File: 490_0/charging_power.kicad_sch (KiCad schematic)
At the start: 32 parts, among them J8 S2B-XH-A, J9 USB_C_Receptacle_USB2.0_16P, SW2 SW_Push, SW3 SW_Push, U4 MP2632BGR-Z

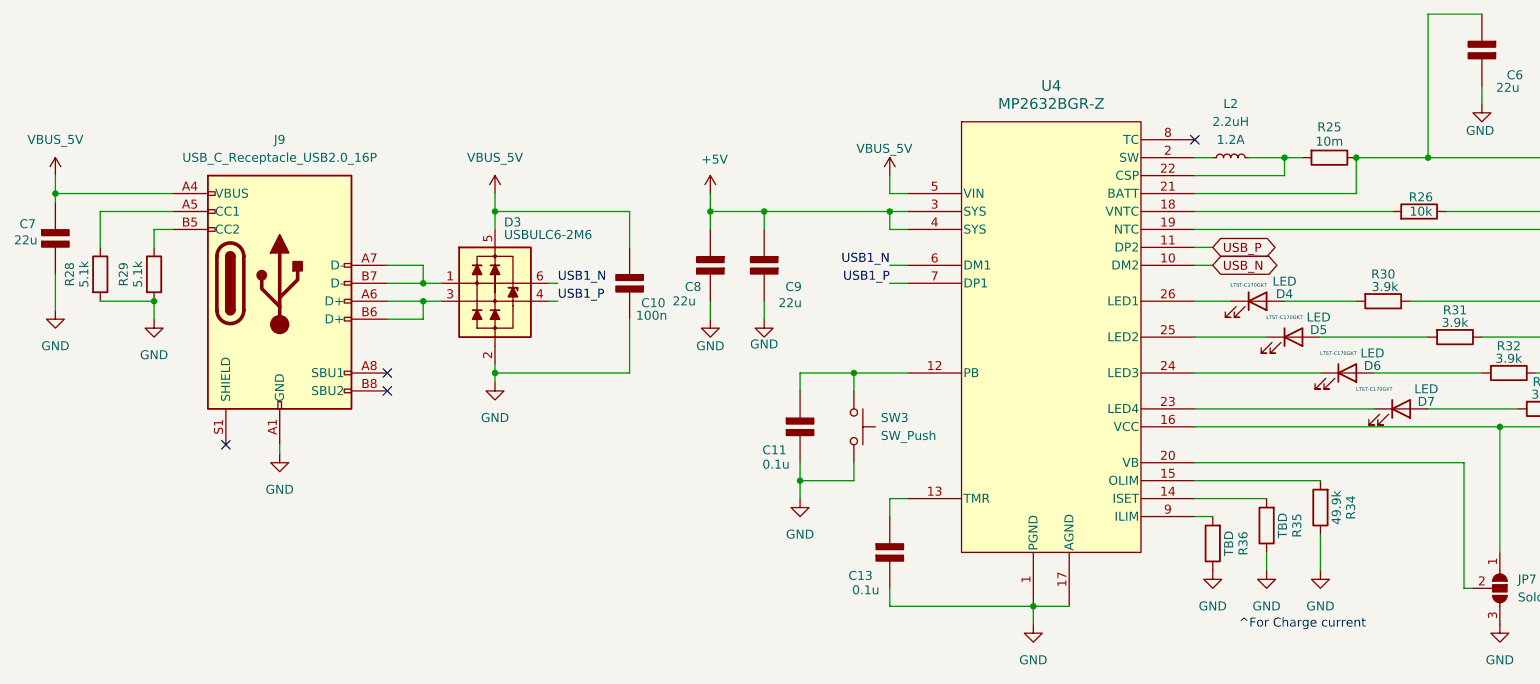
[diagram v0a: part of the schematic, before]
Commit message: changed PCB block diagram
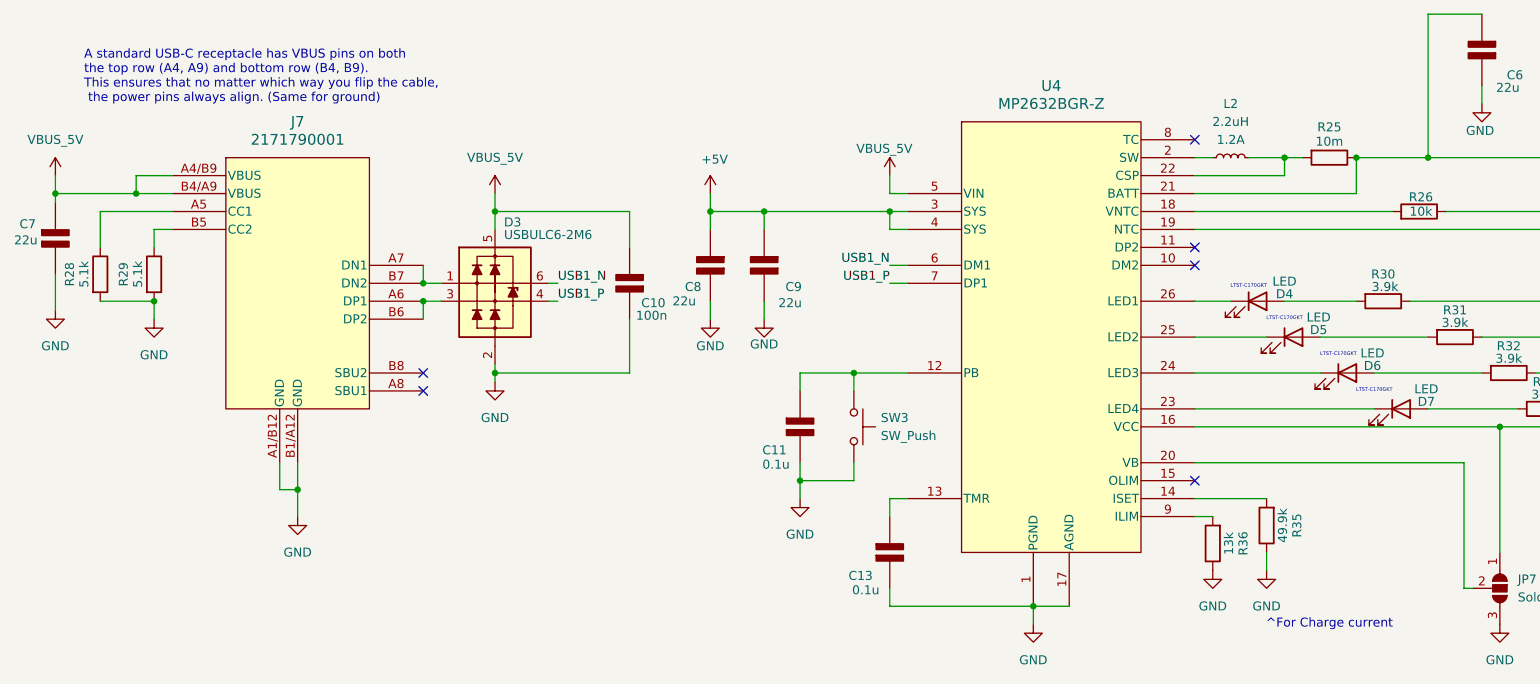
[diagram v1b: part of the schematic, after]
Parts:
- removed J9: USB_C_Receptacle_USB2.0_16P, symbol Connector:USB_C_Receptacle_USB2.0_16P
- removed R34: 49.9k, symbol Device:R
- added J7: 2171790001, 2171790001_MOL, symbol capstone_parts:2171790001
- R35: value TBD -> 49.9k
- R36: value TBD -> 13k
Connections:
- net GND: now also J7.A1/B12 (GND), J7.B1/A12 (GND)
- net VBUS_5V: now also J7.A4/B9 (VBUS), J7.B4/A9 (VBUS)
- net at R29.1: now also J7.B5 (CC2)
- net at R28.1: now also J7.A5 (CC1)
- net at D3.3 (L2): now also J7.A6 (DP1), J7.B6 (DP2)
- net at D3.1 (L1): now also J7.A7 (DN1), J7.B7 (DN2)
- net USB_N: no longer names the net of U4.10 (DM2)
- net USB_P: no longer names the net of U4.11 (DP2)
- no-connect marks 4 -> 6
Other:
- note added: "A standard USB-C receptacle has VBUS pins on both the top row (A4, A9) and bottom row (B4, B9). This ensures that no matter which way you flip the cable, the power pins always align. (Same for ground)"

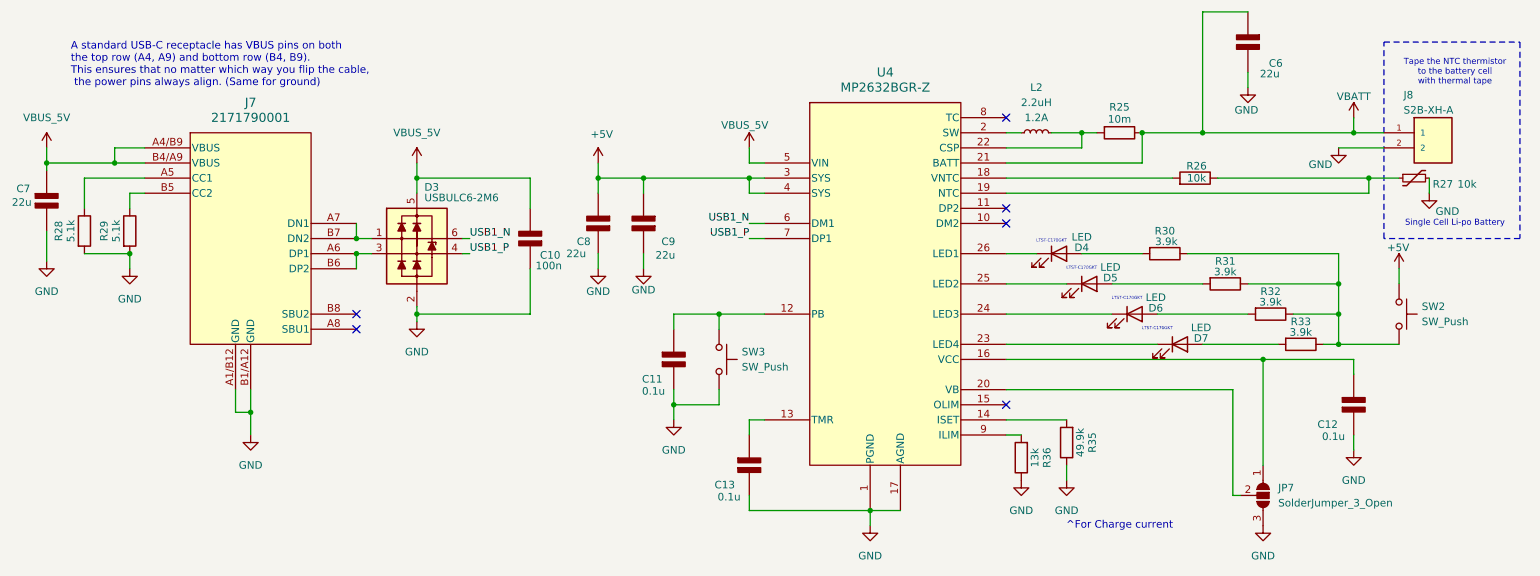
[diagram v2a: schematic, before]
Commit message: Schematic layout update
- applied hierarchical labels
- cleaned up the schematic
- finalized CM4 connections
- checked cm4 connections
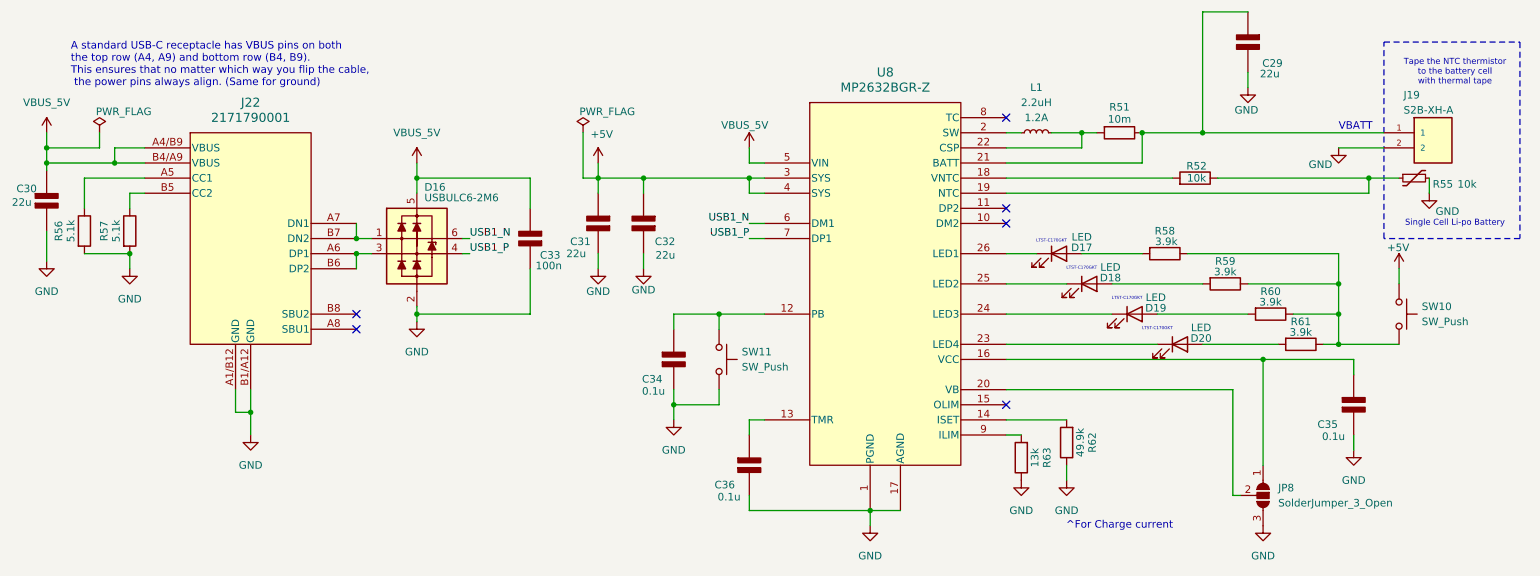
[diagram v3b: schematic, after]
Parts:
- renumbered C6 to C29, C7 to C30, C8 to C31, C9 to C32, C10 to C33, C11 to C34, C12 to C35, C13 to C36, D3 to D16, D4 to D17, D5 to D18, D6 to D19, D7 to D20, J8 to J19, J7 to J22, JP7 to JP8, L2 to L1, R25 to R51, R26 to R52, R27 to R55, R28 to R56, R29 to R57, R30 to R58, R31 to R59, R32 to R60, R33 to R61, R35 to R62, R36 to R63, SW2 to SW10, SW3 to SW11, U4 to U8
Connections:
- net VBATT: no longer names the net of C29.1 (+), J19.1, R51.1, U8.21 (BATT)
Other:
- note added: "VBATT"

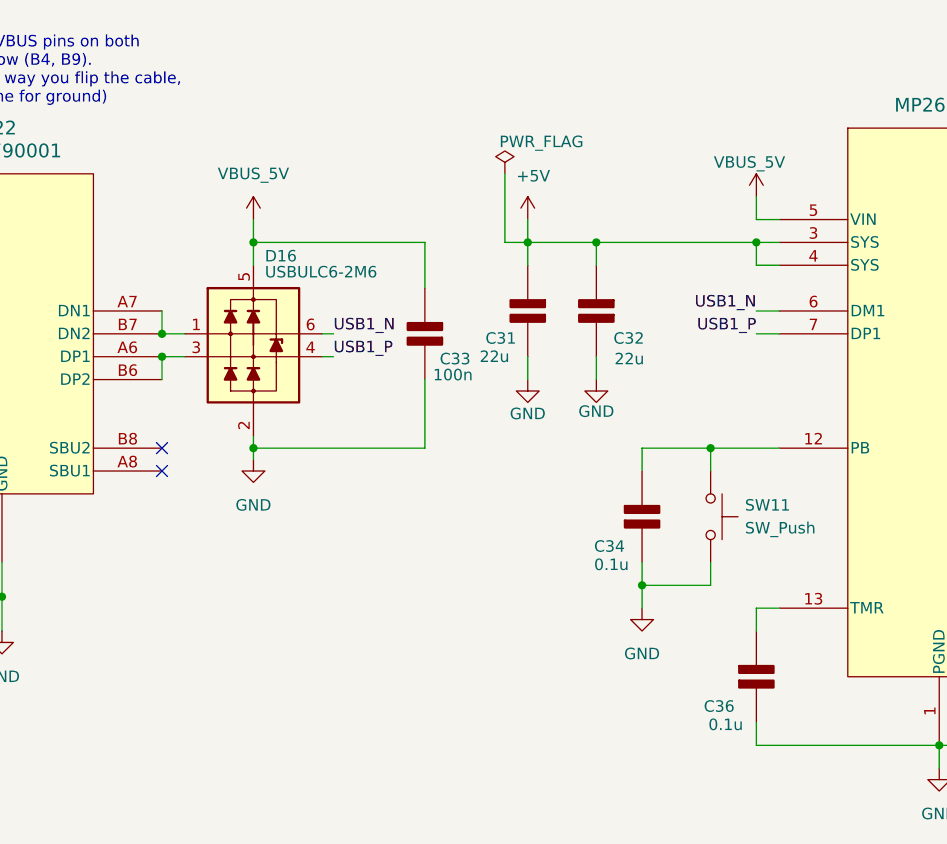
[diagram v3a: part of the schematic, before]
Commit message: Cleaned up global labels
TO DO: power chip change
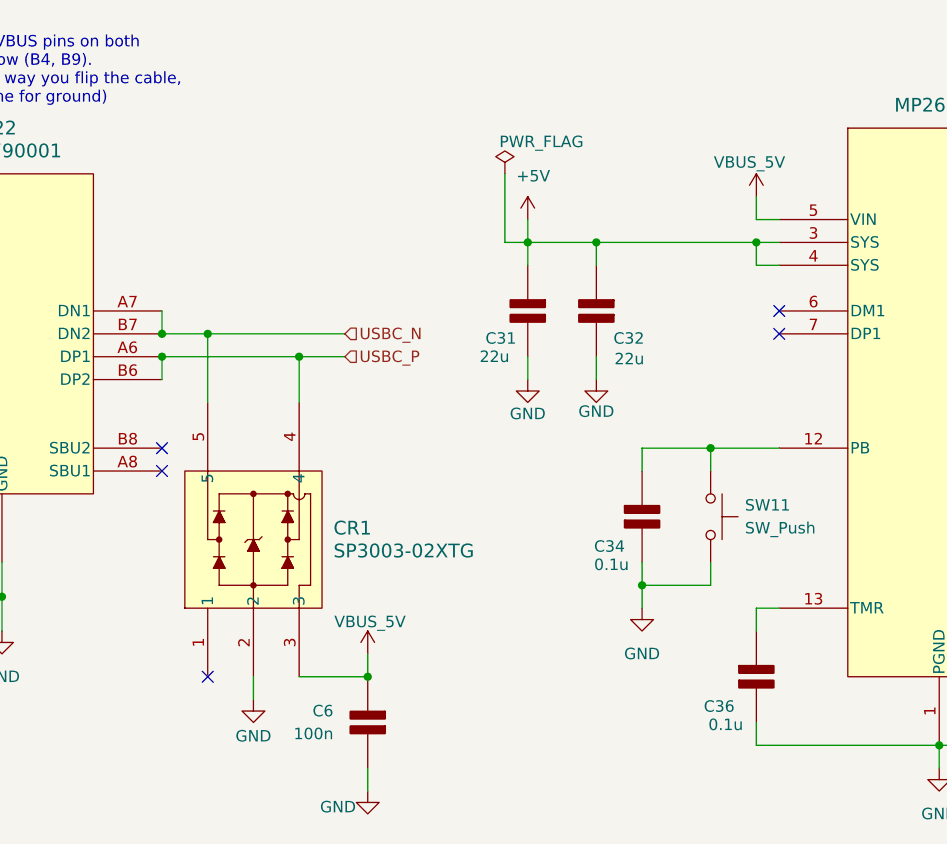
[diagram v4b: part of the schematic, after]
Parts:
- removed C33: 100n, symbol PCM_Elektuur:C
- removed D16: USBULC6-2M6, PCM_Package_TO_SOT_SMD_AKL:SOT-666, symbol PCM_Diode_TVS_AKL:USBLC6-2P6
- added C6: 100n, symbol PCM_Elektuur:C
- added CR1: SP3003-02XTG, SOT553_LTF, symbol capstone_parts:SP3003-02XTG
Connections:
- net GND: now also C6.2 (-), CR1.2
- net VBUS_5V: now also C6.1 (+), CR1.3
- net USBC_P: now reaches J22.A6 (DP1), J22.B6 (DP2)
- net USBC_P: now also CR1.4
- net USBC_N: now reaches J22.A7 (DN1), J22.B7 (DN2)
- net USBC_N: now also CR1.5
- net USB1_N: no longer names the net of U8.6 (DM1)
- net USB1_P: no longer names the net of U8.7 (DP1)
- no-connect marks 6 -> 9

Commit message: Updated power circuit
We now have a 2 cell battery
Chip provides 4A/5V source
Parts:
- added C10, C14: 22u, symbol PCM_Elektuur:C
- added C11, C12, C9: 0.1u, symbol PCM_Elektuur:C
- added C13: 470u, symbol PCM_Elektuur:C
- added C8: 1u, symbol PCM_Elektuur:C
- added D16, D3, D4, D5, D6: LED, symbol Device:LED
- added J18: B3B-XH-A, B3B-XH-A:JST_B3B-XH-A, symbol capstone_parts:B3B-XH-A
- added L2: 2.2u, PCM_SparkFun-Coil:0806, symbol PCM_SparkFun-Coil:2.2uH_0806_1.2A
- added R10: 43k, symbol Device:R
- added R11: 36k, symbol Device:R
- added R12: 82k, symbol Device:R
- added R13: 27k, symbol Device:R
- added R14, R15, R16, R17, R20: 3.9k, symbol Device:R
- added R18, R19, R23: 10k, symbol Device:R
- added R21: 75k, symbol Device:R
- added R22: 24k, symbol Device:R
- added R9: 10k, symbol PCM_SparkFun-Resistor:Thermistor-NTC-10k
- added SW1: SW_Push, symbol Switch:SW_Push
- added TP1: TestPoint, symbol Connector:TestPoint
- added U4: MP2639AGR-Z, symbol capstone_parts:MP2639AGR-Z
- C29, C31, C32, C34, C35, C36, D17, D18, D19, D20, J19, L1, R51, R52, R55, R58, R59, R60, R61, R62, R63, SW10, SW11, U8: now not fitted; now left out of the parts list
- JP8: now not fitted
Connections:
- net VBUS_5V is gone; now on net +5V: C30.1 (+), C6.1 (+), CR1.3, J22.A4/B9 (VBUS), J22.B4/A9 (VBUS), U8.5 (VIN)
- net +5V: now also C13.1 (+), C14.1 (+), R13.1, R21.2, U4.1 (VL)
- net GND: now also C10.1 (+), C12.2 (-), C13.2 (-), C14.2 (-), C8.2 (-), C9.2 (-), J18.3, R10.1, R11.1, R12.1, R18.2, R22.1, R9.2, SW1.2, U4.10 (AGND), U4.5 (PGND)
- new net: R12.2, U4.23 (ISET)
- new net: TP1.1, U4.21 (IB)
- new net: C12.1 (+), SW1.1, U4.7 (PB)
- new net: R10.2, U4.22 (OLIM)
- new net: D5.1 (K), U4.15 (LED3)
- new net: D5.2 (A), R16.2
- new net: D4.1 (K), U4.14 (LED2)
- new net: D4.2 (A), R15.2
- new net: C11.2 (-), L2.1, U4.2 (LX), U4.4 (SW)
- new net: C9.1 (+), U4.11 (TMR)
- new net: D3.1 (K), U4.13 (LED1)
- new net: D3.2 (A), R14.2
- new net: C11.1 (+), U4.6 (BST)
- new net: R14.1, R15.1, R16.1, R17.1, R19.2, R20.1, U4.19 (VNTC)
- new net: J18.2, U4.12 (MID)
- new net: D6.1 (K), U4.16 (LED4)
- new net: R21.1, R22.2, U4.17 (FB)
- new net: R13.2, R18.1, U4.18 (VLIM)
- new net: R19.1, R9.1, U4.20 (NTC)
- new net: R11.2, U4.24 (ILIM)
- new net: R23.1, U4.25 (ACOK), U4.8 (MODE)
- new net: D16.1 (K), U4.26 (CHG)
- new net: C8.1 (+), R23.2, U4.9 (VCC)
- new net: D6.2 (A), R17.2
- new net: D16.2 (A), R20.2
- new net +BATT: C10.2 (-), J18.1, L2.2, U4.3 (VH)
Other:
- note added: ""Anti-Crash" Capacitor (Crucial for CM4)"
- note added: "2 Cell Li-po Battery With thermistor taped on it assemble two 18650 single cell batteries and add the mid point cable between the two"
- note added: "Aluminum Electrolytic (Low ESR)"
- note added: "Charge Current,ISET (23),82 kΩ,~2.6A Charging (Fast for 4Ah cells) Input Limit,ILIM (21),36 kΩ,~3.1A Limit from USB (Safe for most adapters) Discharge Limit,OLIM (22),43 kΩ,~4.9A Limit (for 4A load) Logic Pull-up,ACOK (25),10 kΩ,Standard Pull-up Temp Fake (High),VNTC to NTC,10 kΩ,Part 1 of Voltage Divider Temp Fake (Low),NTC to AGND,10 kΩ,Part 2 of Voltage Divider"
- note added: "USB Inserted: The chip detects 5V on VL. ACOK pulls internal switch to Ground (LOW). -> MODE goes LOW -> Chip enters Charge Mode. USB Removed: ACOK lets go (High Impedance). ->The 10kΩ resistor pulls MODE up to VCC (HIGH). -> Chip enters Discharge Mode."
- note added: "break this pin out to a test point on your PCB. During your initial testing, you can use a multimeter to measure the voltage and calculate exactly how much "fuel" your robot is consuming without having to cut wires to insert an ammeter."
- moved on the sheet: C30, C6, CR1, J22, R56, R57
